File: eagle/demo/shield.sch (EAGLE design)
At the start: 15 parts, among them X1 MALE_2X1-T-VERTICAL, X301 MALE_2X1-T-VERTICAL, X302 MALE_2X10-T-VERTICAL_2.54MM

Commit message: kbd module
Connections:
- net CORE_CLK renamed MCU_CLK
- net CORE_QD renamed MCU_QD
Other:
- note added: "?"

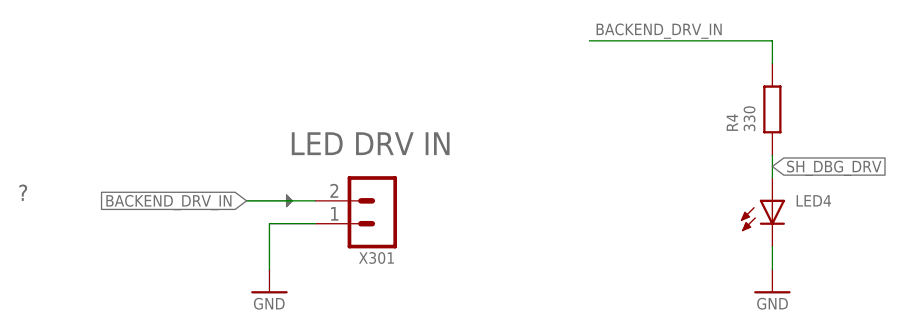
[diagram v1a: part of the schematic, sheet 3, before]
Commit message: fixed prefixes
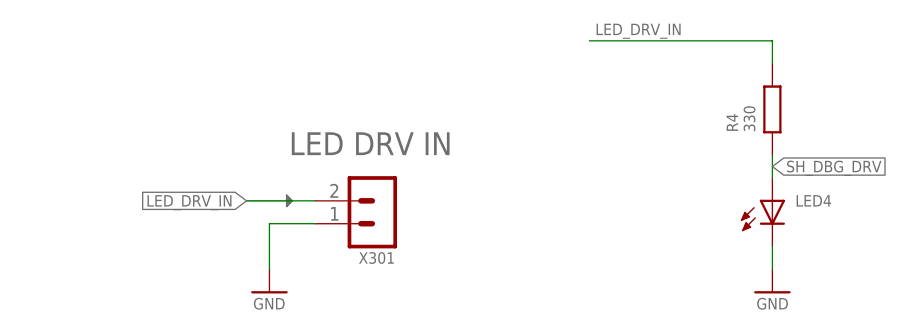
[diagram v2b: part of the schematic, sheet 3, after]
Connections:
- net BACKEND_DRV_IN renamed LED_DRV_IN
- net BACKEND_KBD_OUT renamed KBD_OUT
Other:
- note removed: "?"
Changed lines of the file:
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@@
 </segment>
 </net>
-<net name="BACKEND_DRV_IN" class="0">
+<net name="LED_DRV_IN" class="0">
 <segment>
 <pinref part="N1" gate="G$1" pin="1"/>
@@
 </segment>
 </net>
-<net name="BACKEND_KBD_OUT" class="0">
+<net name="KBD_OUT" class="0">
 <segment>
 <pinref part="N2" gate="G$1" pin="1"/>
@@
 <description>connector LED driver module</description>
 <plain>
-<text x="139.7" y="60.96" size="1.778" layer="97">?</text>
 </plain>
 <instances>
@@
 </segment>
 </net>
-<net name="BACKEND_DRV_IN" class="0">
+<net name="LED_DRV_IN" class="0">
 <segment>
 <pinref part="R4" gate="G$1" pin="2"/>
@@
 </segment>
 </net>
-<net name="BACKEND_KBD_OUT" class="0">
+<net name="KBD_OUT" class="0">
 <segment>
 <pinref part="R3" gate="G$1" pin="2"/>

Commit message: fix partcodes
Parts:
- LED301: value (none) -> green; FUNCTION (none) -> DRV ON; PART_CODE_BEL (none) -> LED_PAC_S_0805_VAL_green
- LED401: value (none) -> red; FUNCTION (none) -> BUTTON PRESSED; PART_CODE_BEL (none) -> LED_PAC_S_0805_VAL_red
- R301, R401: PART_CODE_BEL (none) -> R_PAC_S_0805_VAL_330
- X101: PART_CODE_BEL (none) -> X_PAC_T_MALE_2X10_VERTICAL_PITCH_2mm54
- renumbered FD1 to FD101, FD2 to FD102, H1 to H103, H2 to H104, H3 to H101, H4 to H102, LED3 to LED401, LED4 to LED301, N1 to N201, N2 to N202, R3 to R401, R4 to R301, X1 to X401, X302 to X101
